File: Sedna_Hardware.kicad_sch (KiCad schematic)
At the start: 46 parts, among them J1 PJ-102A, J10 Conn_01x03, J11 Conn_01x03, J2 Screw_Terminal_01x02, J3 Screw_Terminal_01x02, J4 Conn_01x02, J5 Conn_02x05_Odd_Even, J6 Conn_01x03, J7 0878340619, J8 Conn_01x14, J9 Conn_01x03, K1 ALDP105W, K2 ALDP105W, Q1 2N7000-D75Z, Q2 2N7000-D75Z, U1 LD1117V33, U2 ESP32-WROOM-32D-N16, U3 LM6511IMX/NOPB

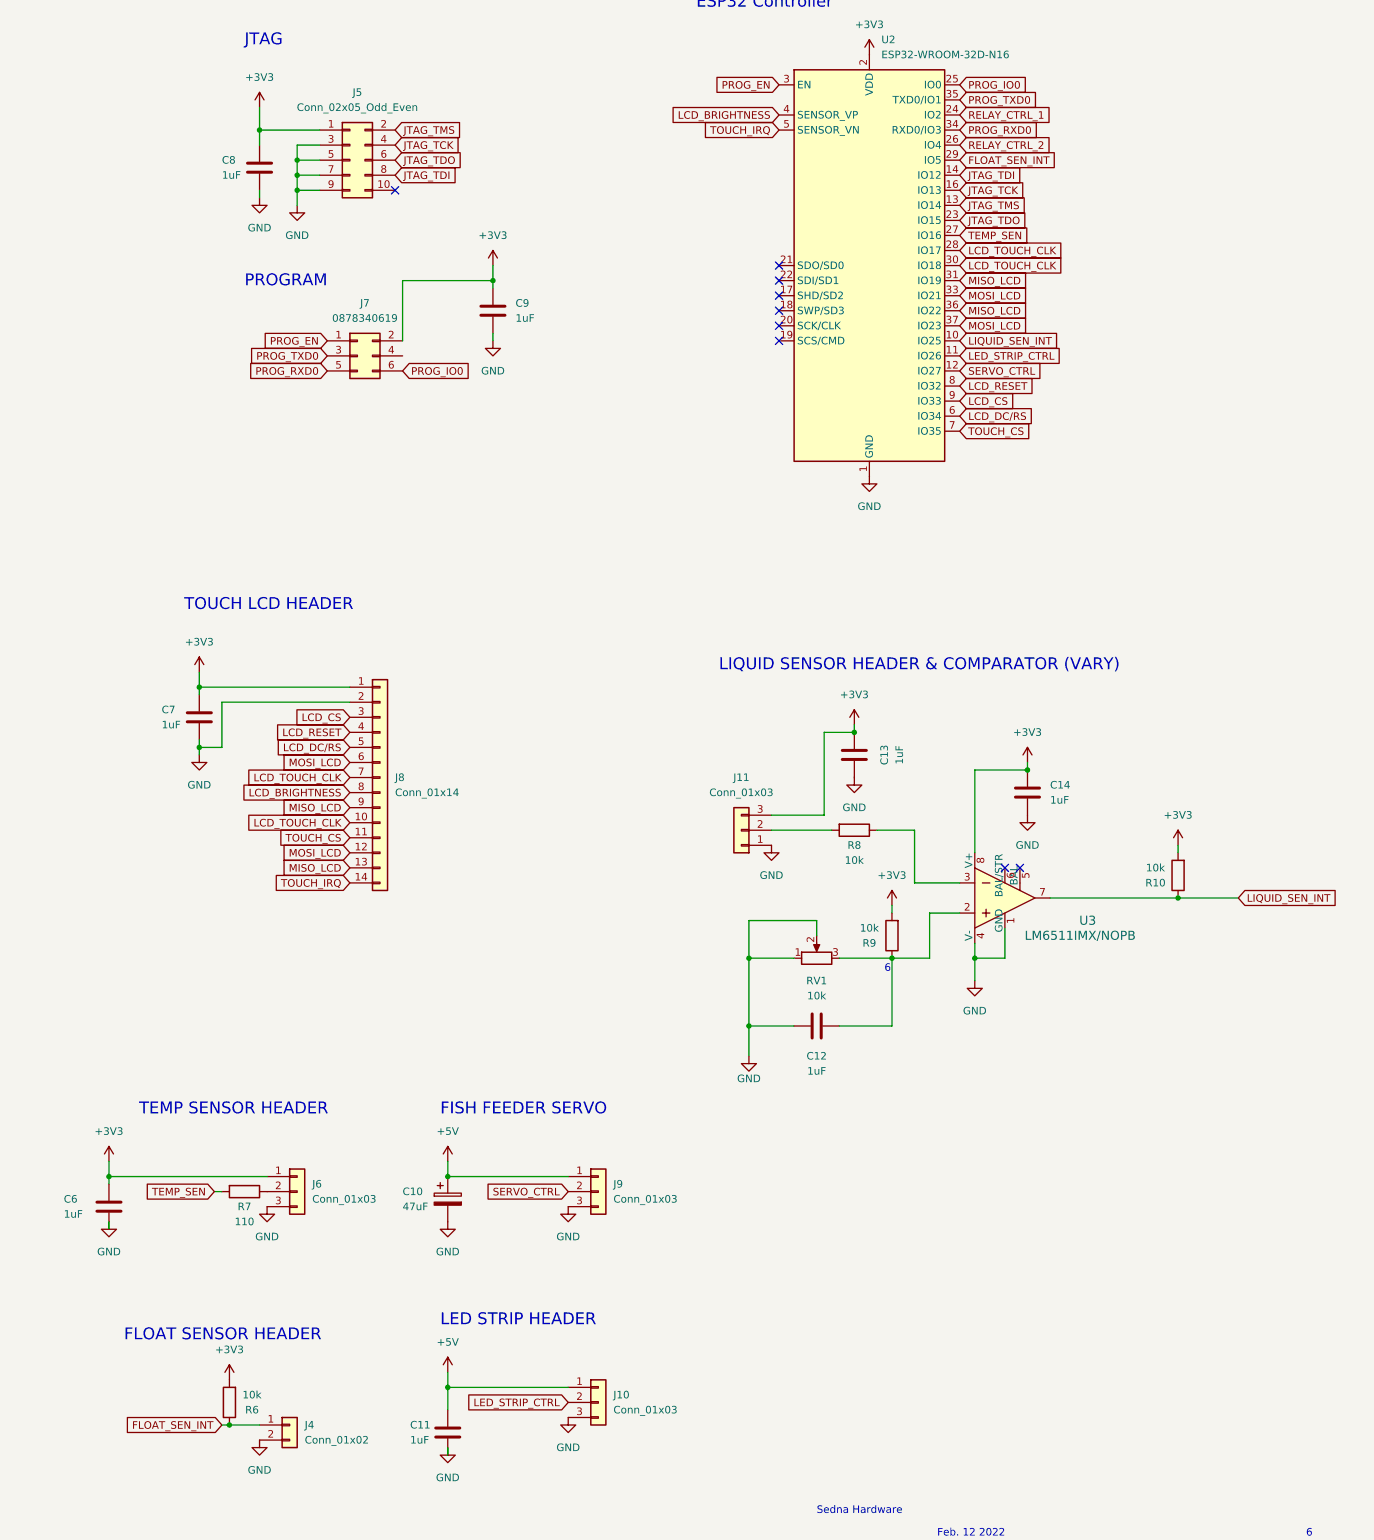
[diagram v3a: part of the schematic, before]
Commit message: Replaced ESP32-WROOM-32E with ESP32-WROOM-32D. Stock issues
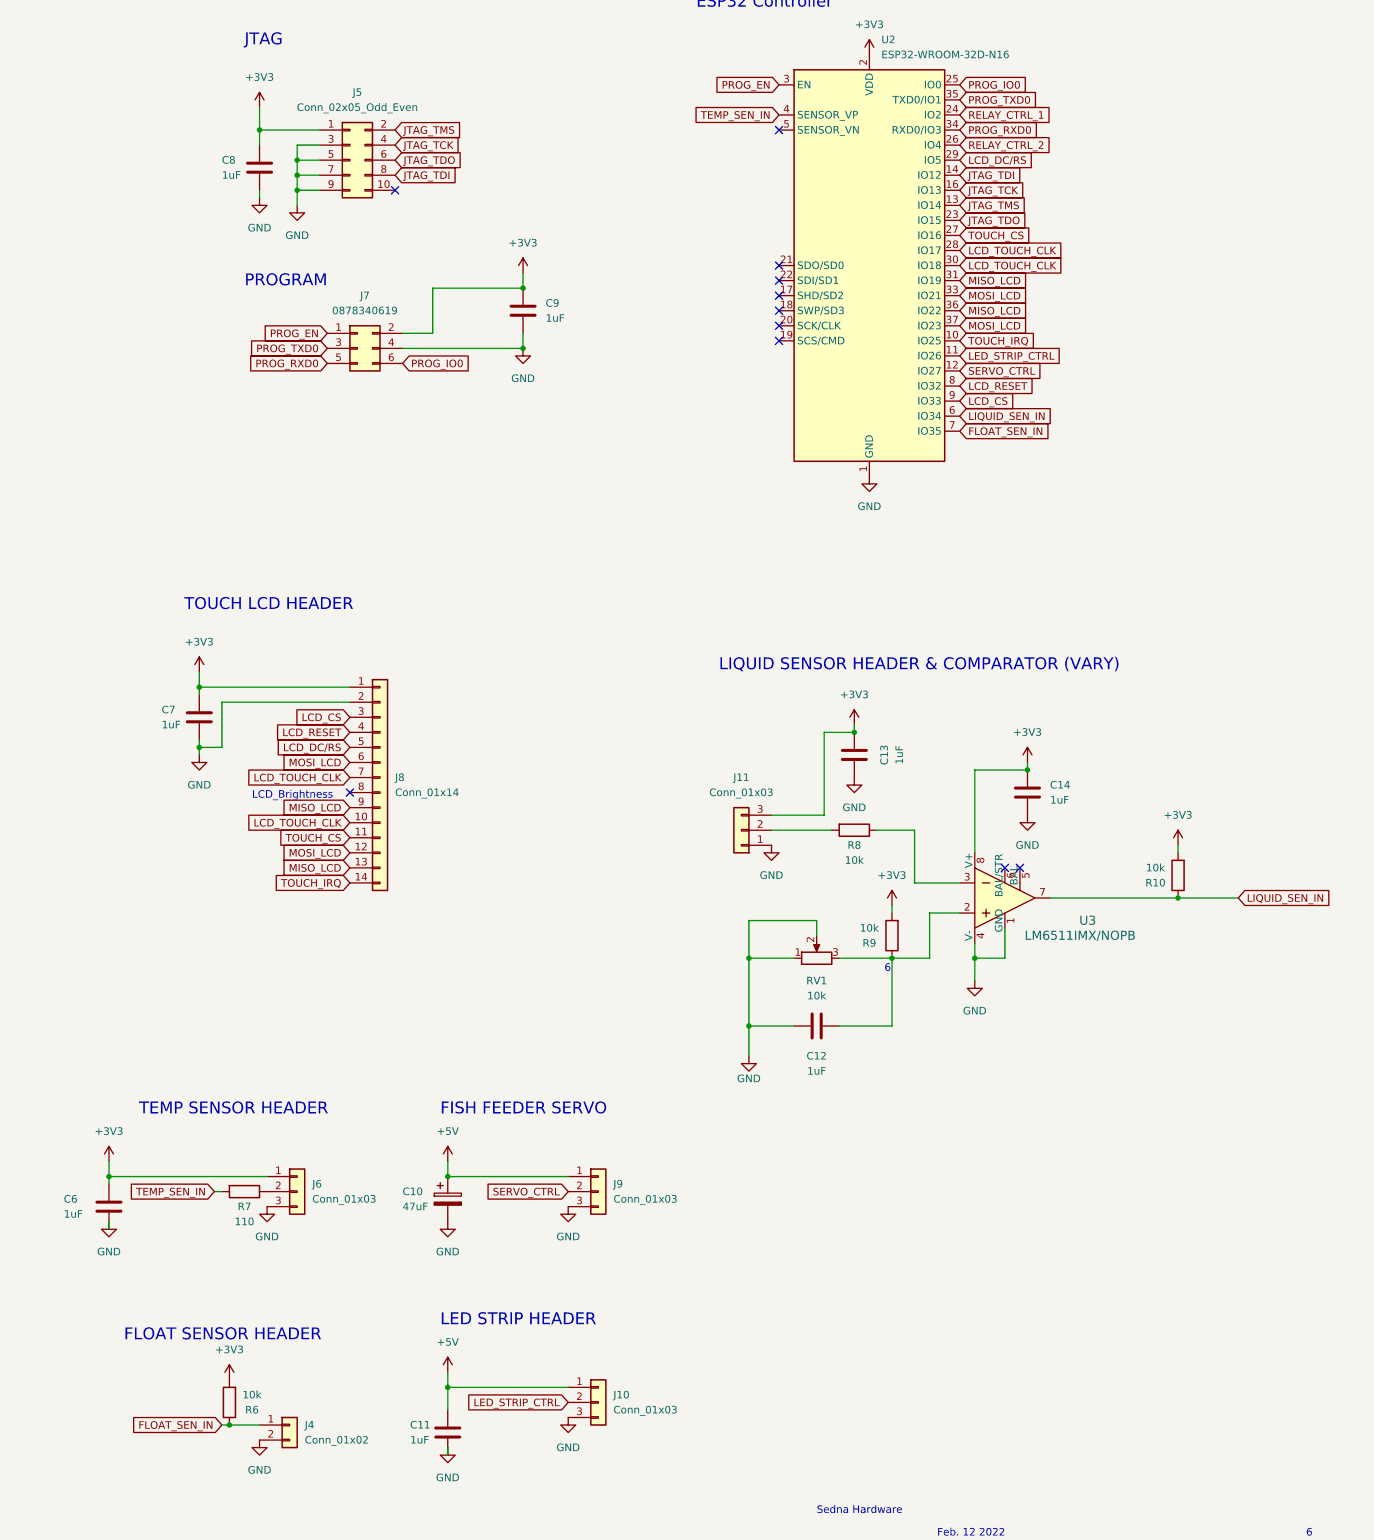
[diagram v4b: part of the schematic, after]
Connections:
- net GND: now also J7.4 (Pin_4)
- net LCD_DC/RS: now also U2.29 (IO5); no longer U2.6 (IO34)
- net TOUCH_CS: now also U2.27 (IO16); no longer U2.7 (IO35)
- net TOUCH_IRQ: now also U2.10 (IO25); no longer U2.5 (SENSOR_VN)
- net FLOAT_SEN_INT renamed FLOAT_SEN_IN
- net FLOAT_SEN_IN: now also U2.7 (IO35); no longer U2.29 (IO5)
- net LCD_BRIGHTNESS: no longer names the net of J8.8 (Pin_8)
- net LCD_BRIGHTNESS: no longer U2.4 (SENSOR_VP)
- net LIQUID_SEN_INT renamed LIQUID_SEN_IN
- net LIQUID_SEN_IN: now also U2.6 (IO34); no longer U2.10 (IO25)
- net TEMP_SEN renamed TEMP_SEN_IN
- net TEMP_SEN_IN: now also U2.4 (SENSOR_VP); no longer U2.27 (IO16)
- no-connect marks 9 -> 11
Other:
- note added: "LCD_Brightness"
- moved on the sheet: C9, J7

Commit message: Fixed schematic and pcb placement. added mounting holes
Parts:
- added H1, H2, H3, H4: Mounting_Hole, MountingHole:MountingHole_3.5mm, symbol Connector:Conn_01x01_Male
- J10, J9: value Conn_01x03 -> 2-644803-3; footprint Connector_PinHeader_2.54mm:PinHeader_1x03_P2.54mm_Horizontal -> 2-644803-3:TE_2-644803-3; Category (none) -> CONN; DK_Datasheet_Link (none) -> https://www.te.com/commerce/DocumentDelivery/DDEController?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; DK_Detail_Page (none) -> https://www.digikey.ca/en/products/detail/te-connectivity-a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; Digi-Key_PN (none) -> A30925-ND; Family (none) -> CONN; MPN (none) -> 2-644803-3; Manufacturer (none) -> TE Connectivity AMP Connectors; Mating_CONN (none) -> 3-640469-3; Mating_DK_Page (none) -> https://www.digikey.ca/en/products/detail/te-connectivity-a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; Mating_MPN (none) -> 3-640469-3; Status (none) -> active
- J11: value Conn_01x03 -> 2-644488-3; footprint Connector_PinHeader_2.54mm:PinHeader_1x03_P2.54mm_Horizontal -> 2-644488-3:TE_2-644488-3; Category (none) -> CONN; DK_Datasheet_Link (none) -> https://www.te.com/commerce/DocumentDelivery/DDEController?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; DK_Detail_Page (none) -> https://www.digikey.ca/en/products/detail/te-connectivity-a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; Digi-Key_PN (none) -> A30901-ND; Family (none) -> CONN; MPN (none) -> 2-644488-3; Manufacturer (none) -> TE Connectivity AMP Connectors; Mating_CONN (none) -> 3-640468-3; Mating_DK_Page (none) -> https://www.digikey.ca/en/products/detail/te-connectivity-a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; Mating_MPN (none) -> 3-640468-3; Status (none) -> active
- J4: value Conn_01x02 -> 2-644488-2; footprint Connector_PinHeader_2.54mm:PinHeader_1x02_P2.54mm_Horizontal -> 2-644488-2:TE_2-644488-2; Category (none) -> CONN; DK_Datasheet_Link (none) -> https://www.te.com/commerce/DocumentDelivery/DDEController?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; DK_Detail_Page (none) -> https://www.digikey.ca/en/products/detail/te-connectivity-a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; Digi-Key_PN (none) -> A30900-ND; Family (none) -> CONN; MPN (none) -> 2-644488-2; Manufacturer (none) -> TE Connectivity AMP Connectors; Mating_Conn (none) -> 3-644043-2; Mating_DK_Page (none) -> https://www.digikey.ca/en/products/detail/te-connectivity-a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; Mating_MPN (none) -> 3-644043-2; Status (none) -> active
- J5: value Conn_02x05_Odd_Even -> 61201021721
- J6: value Conn_01x03 -> 5-103634-2; footprint Connector_PinHeader_2.54mm:PinHeader_1x03_P2.54mm_Horizontal -> 5-103634-2:TE_5-103634-2; Category (none) -> CONN HEADER R/A 3POS 2.54MM; DK_Datasheet_Link (none) -> https://www.te.com/commerce/DocumentDelivery/DDEController?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; DK_Detail_Page (none) -> https://www.digikey.ca/en/products/detail/te-connectivity-a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; Digi-Key_PN (none) -> A33859-ND; Family (none) -> CONN; MPN (none) -> 5-103634-2; Manufacturer (none) -> TE Connectivity AMP Connectors; Mating_CONN (none) -> 487526-2; Mating_DK_Page (none) -> https://www.digikey.ca/en/products/detail/te-connectivity-a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; Mating_MPN (none) -> 487526-2; Status (none) -> active
- J7: MPN Molex -> 0878340619
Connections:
- net at R8.1: now also J11.2 (Pin_2); no longer U3.3
- net at R8.2: now also U3.3; no longer J11.2 (Pin_2)
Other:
- note added: "1"
- note added: "Authour: Liam-Thomas Flynn & Teng Zhao"
- moved on the sheet: C1, C10, C11, C12, C13, C14, C2, C3, C4, C5, C6, C7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

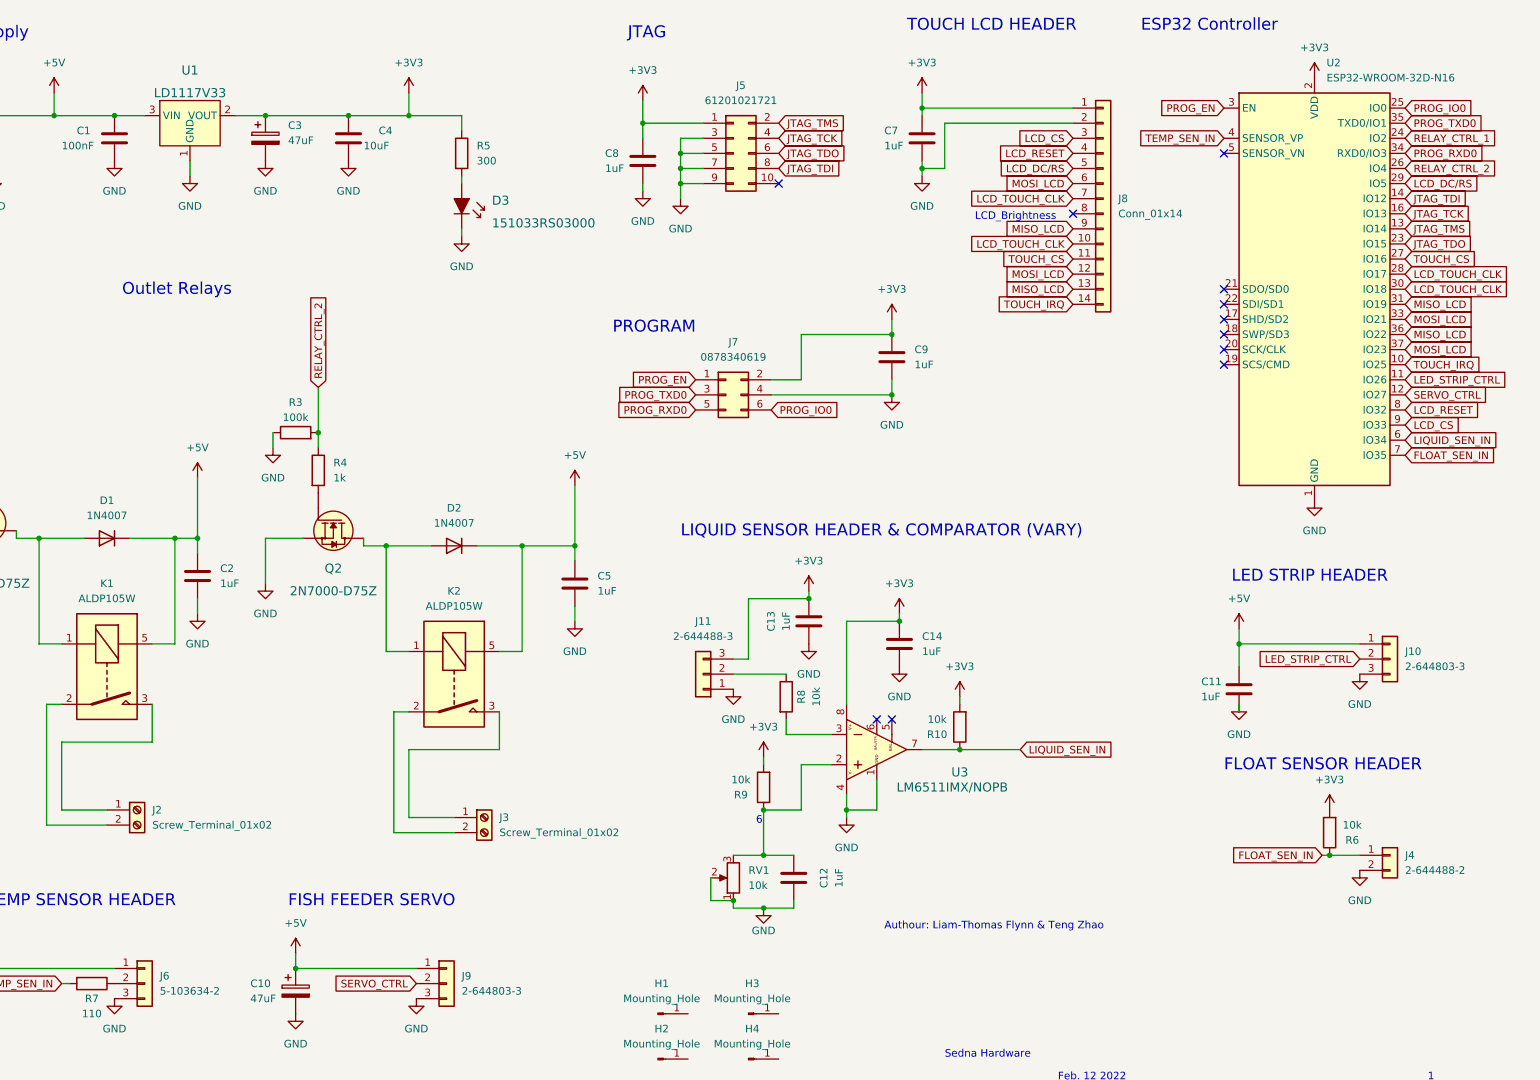
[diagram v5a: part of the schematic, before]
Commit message: fixed SPI connecion to LCD. Add correct screw terminals
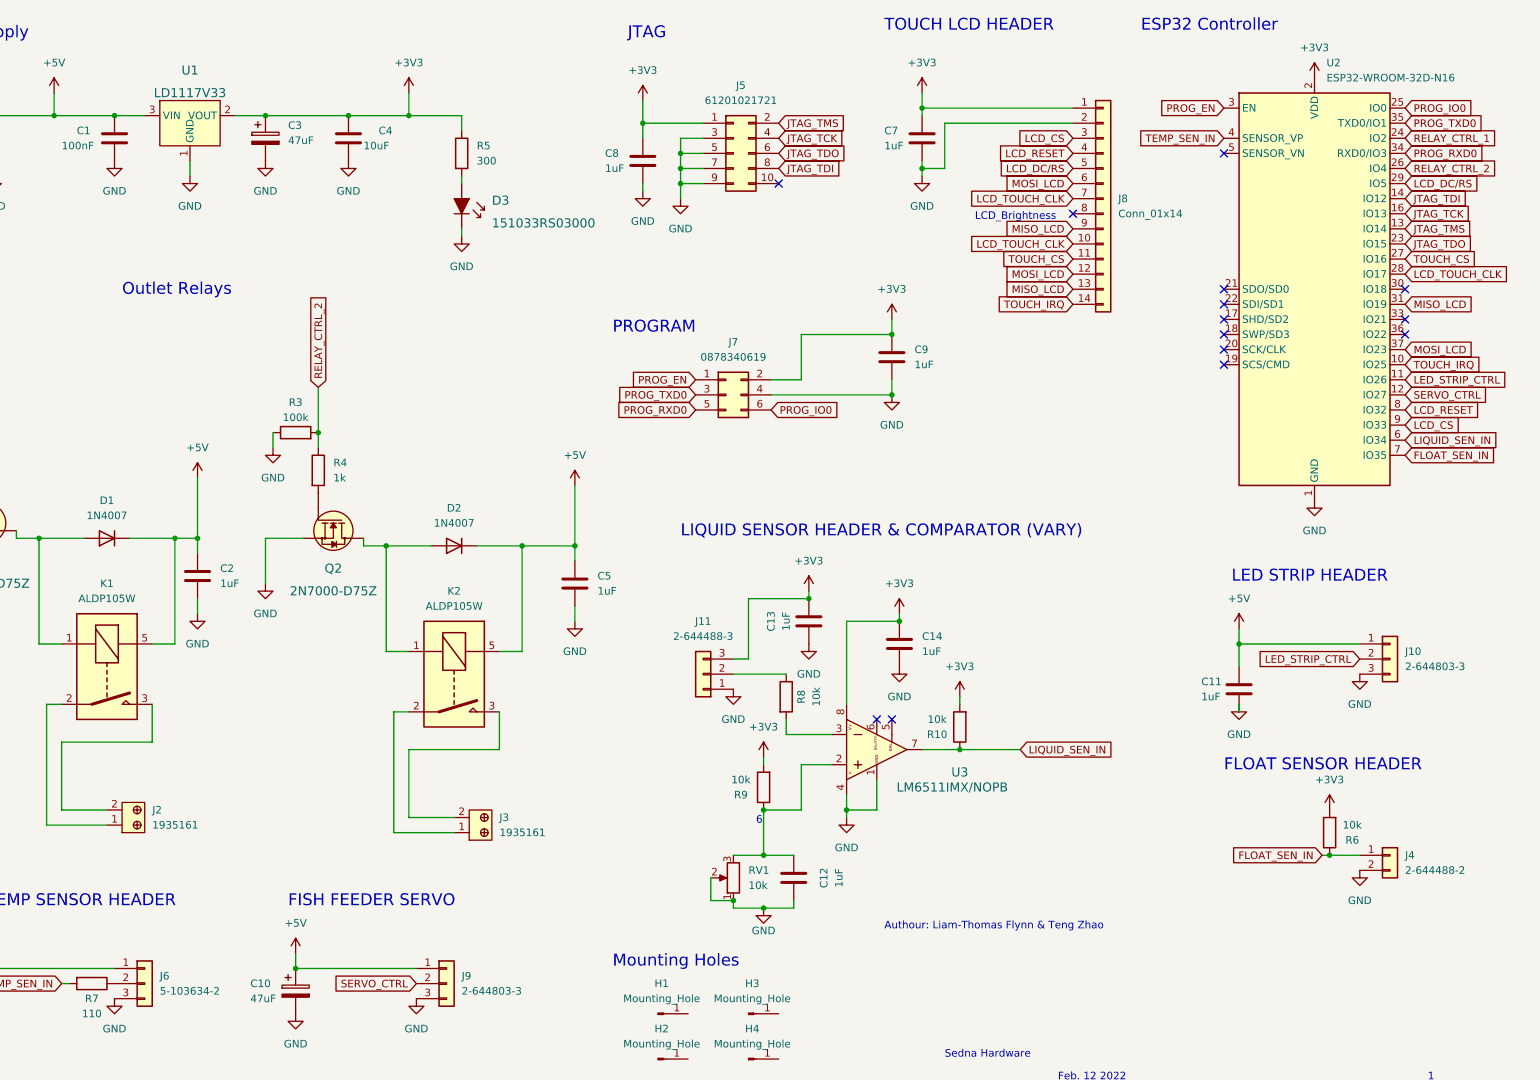
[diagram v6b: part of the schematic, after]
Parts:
- removed J2, J3: Screw_Terminal_01x02, TerminalBlock:TerminalBlock_Altech_AK300-2_P5.00mm, symbol Connector:Screw_Terminal_01x02
- added J2, J3: 1935161, digikey-footprints:Terminal_Block_D1.3mm_P5mm, symbol dk_Terminal-Blocks-Wire-to-Board:1935161
- U3: footprint digikey-footprints:DIP-8_W7.62mm -> Package_SO:SOIC-8_3.9x4.9mm_P1.27mm
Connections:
- net LCD_TOUCH_CLK: no longer U2.30 (IO18)
- net MISO_LCD: no longer U2.36 (IO22)
- net MOSI_LCD: no longer U2.33 (IO21)
- net at K1.3: now also J2.2
- net at K1.2: now also J2.1
- net at K2.2: now also J3.1
- net at K2.3: now also J3.2
- no-connect marks 11 -> 14
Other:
- note added: "Mounting Holes"
